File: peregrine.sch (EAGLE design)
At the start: 77 parts, among them IC2 LMV358IDGKR, J1 USB MICRO, Q1 BSS123, Q10 BSS123, Q11 BSS123, Q2 BSS123, U1 ITG-3200, U2 ADXL345, U5 ATMEGA32U4-XUAU, Y1 16MHz KX-7

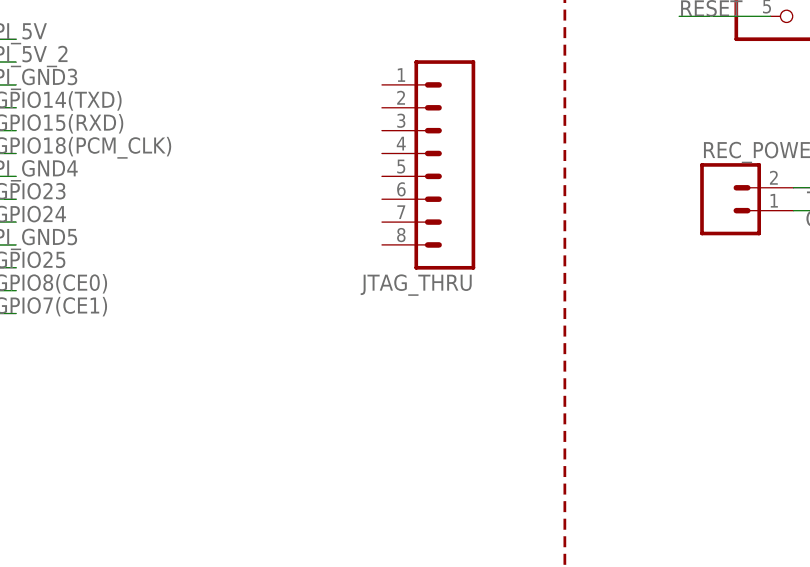
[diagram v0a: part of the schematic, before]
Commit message: Fixed silk
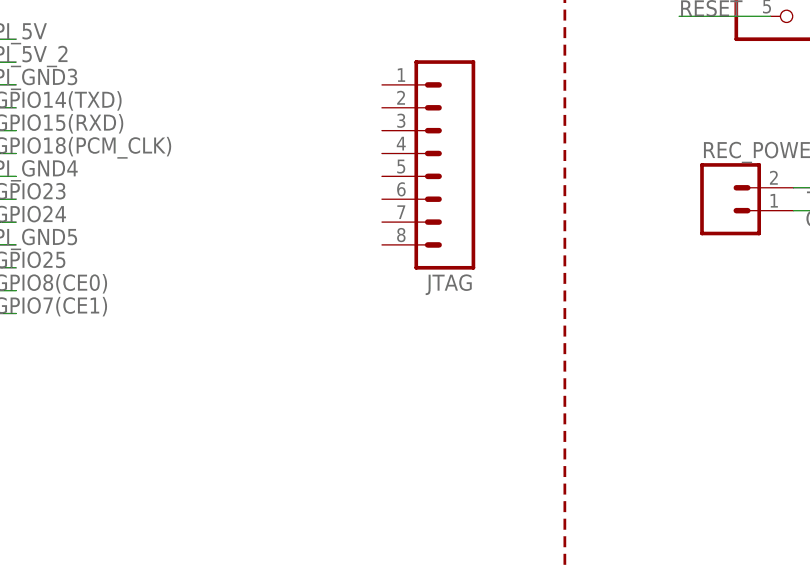
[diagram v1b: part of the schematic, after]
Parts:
- renumbered JTAG_THRU to JTAG
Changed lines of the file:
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@@
 <part name="C14" library="SparkFun" deviceset="CAP" device="0402-CAP" value="0.1uF"/>
 <part name="GND16" library="SparkFun" deviceset="GND" device=""/>
-<part name="JTAG_THRU" library="SparkFun" deviceset="M08" device="LOCK"/>
+<part name="JTAG" library="SparkFun" deviceset="M08" device="LOCK"/>
 <part name="SJ5" library="jumper" deviceset="SJ" device=""/>
 <part name="SJ6" library="jumper" deviceset="SJ" device=""/>
@@
 </instance>
 <instance part="GND16" gate="1" x="-15.24" y="-43.18"/>
-<instance part="JTAG_THRU" gate="G$1" x="124.46" y="83.82" rot="R180"/>
+<instance part="JTAG" gate="G$1" x="124.46" y="83.82" rot="R180"/>
 <instance part="SJ5" gate="1" x="231.14" y="48.26"/>
 <instance part="SJ6" gate="1" x="231.14" y="43.18"/>

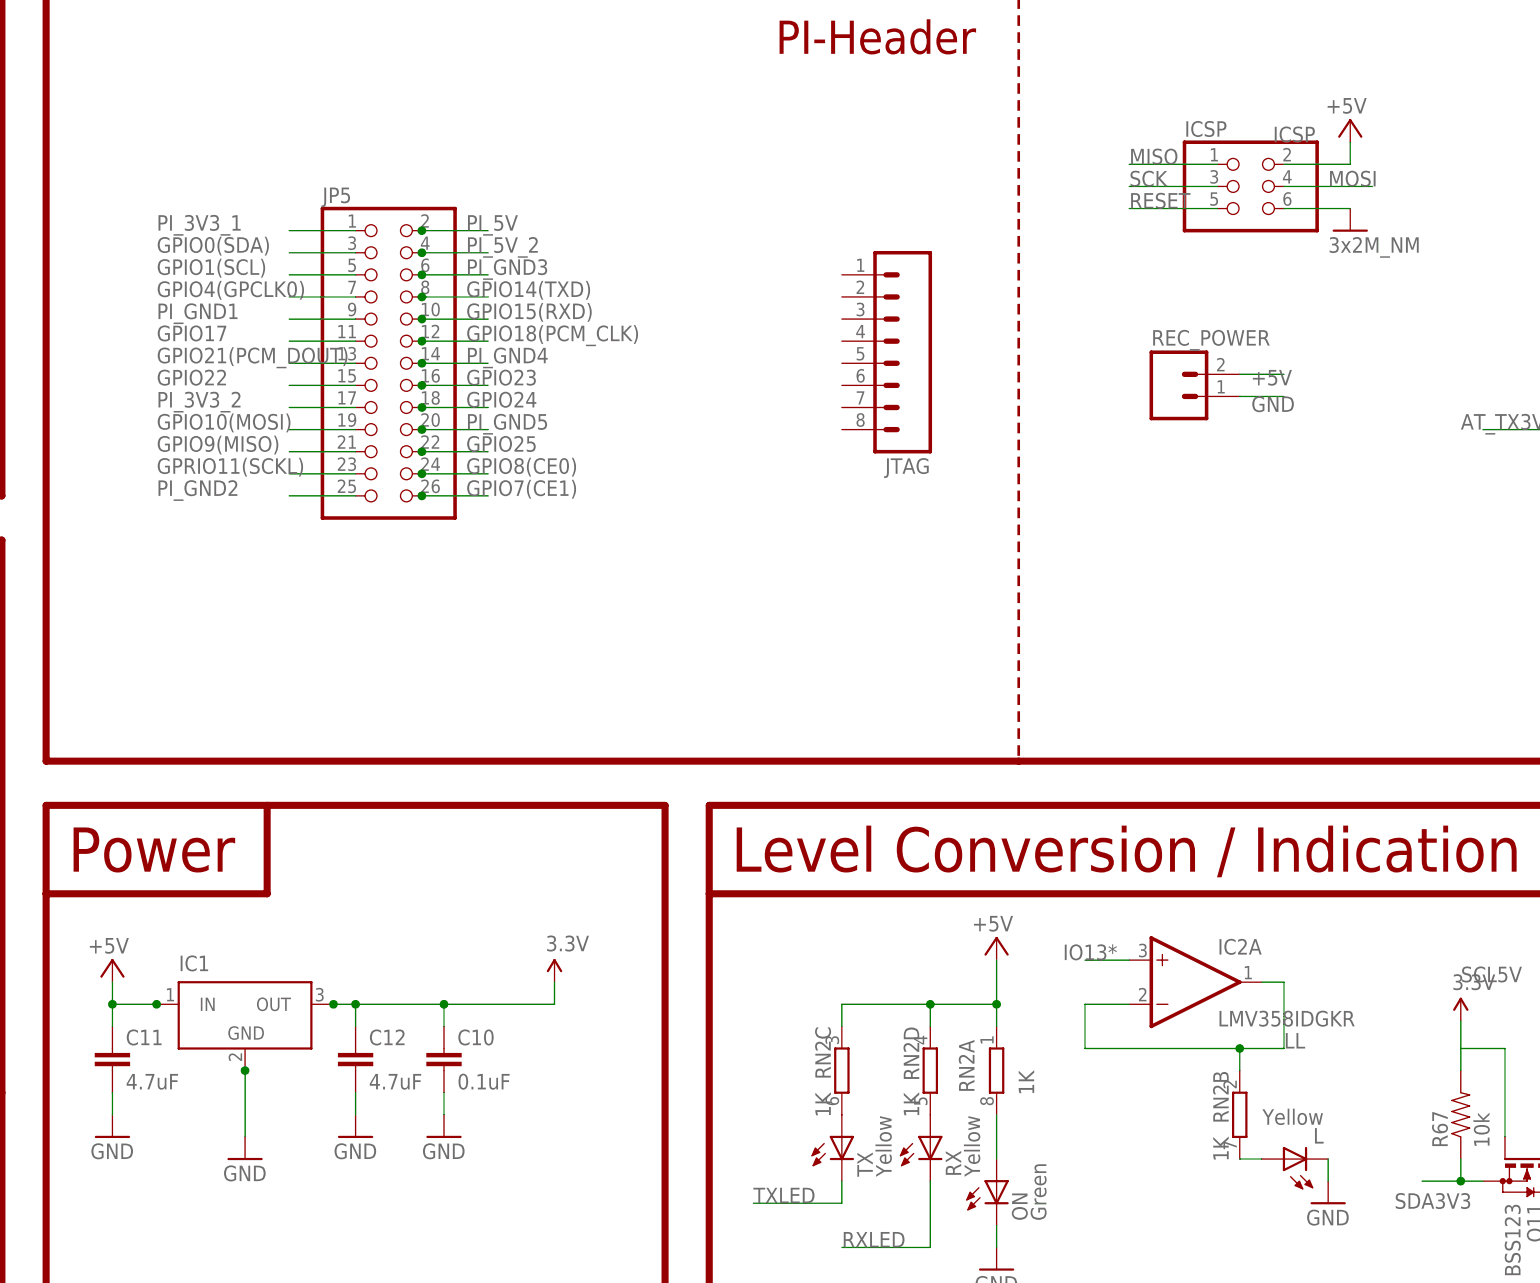
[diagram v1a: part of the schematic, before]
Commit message: Moderate Re-Route.`
Everything on top layer, a bit more pretty, some schematic changes, new
silk.
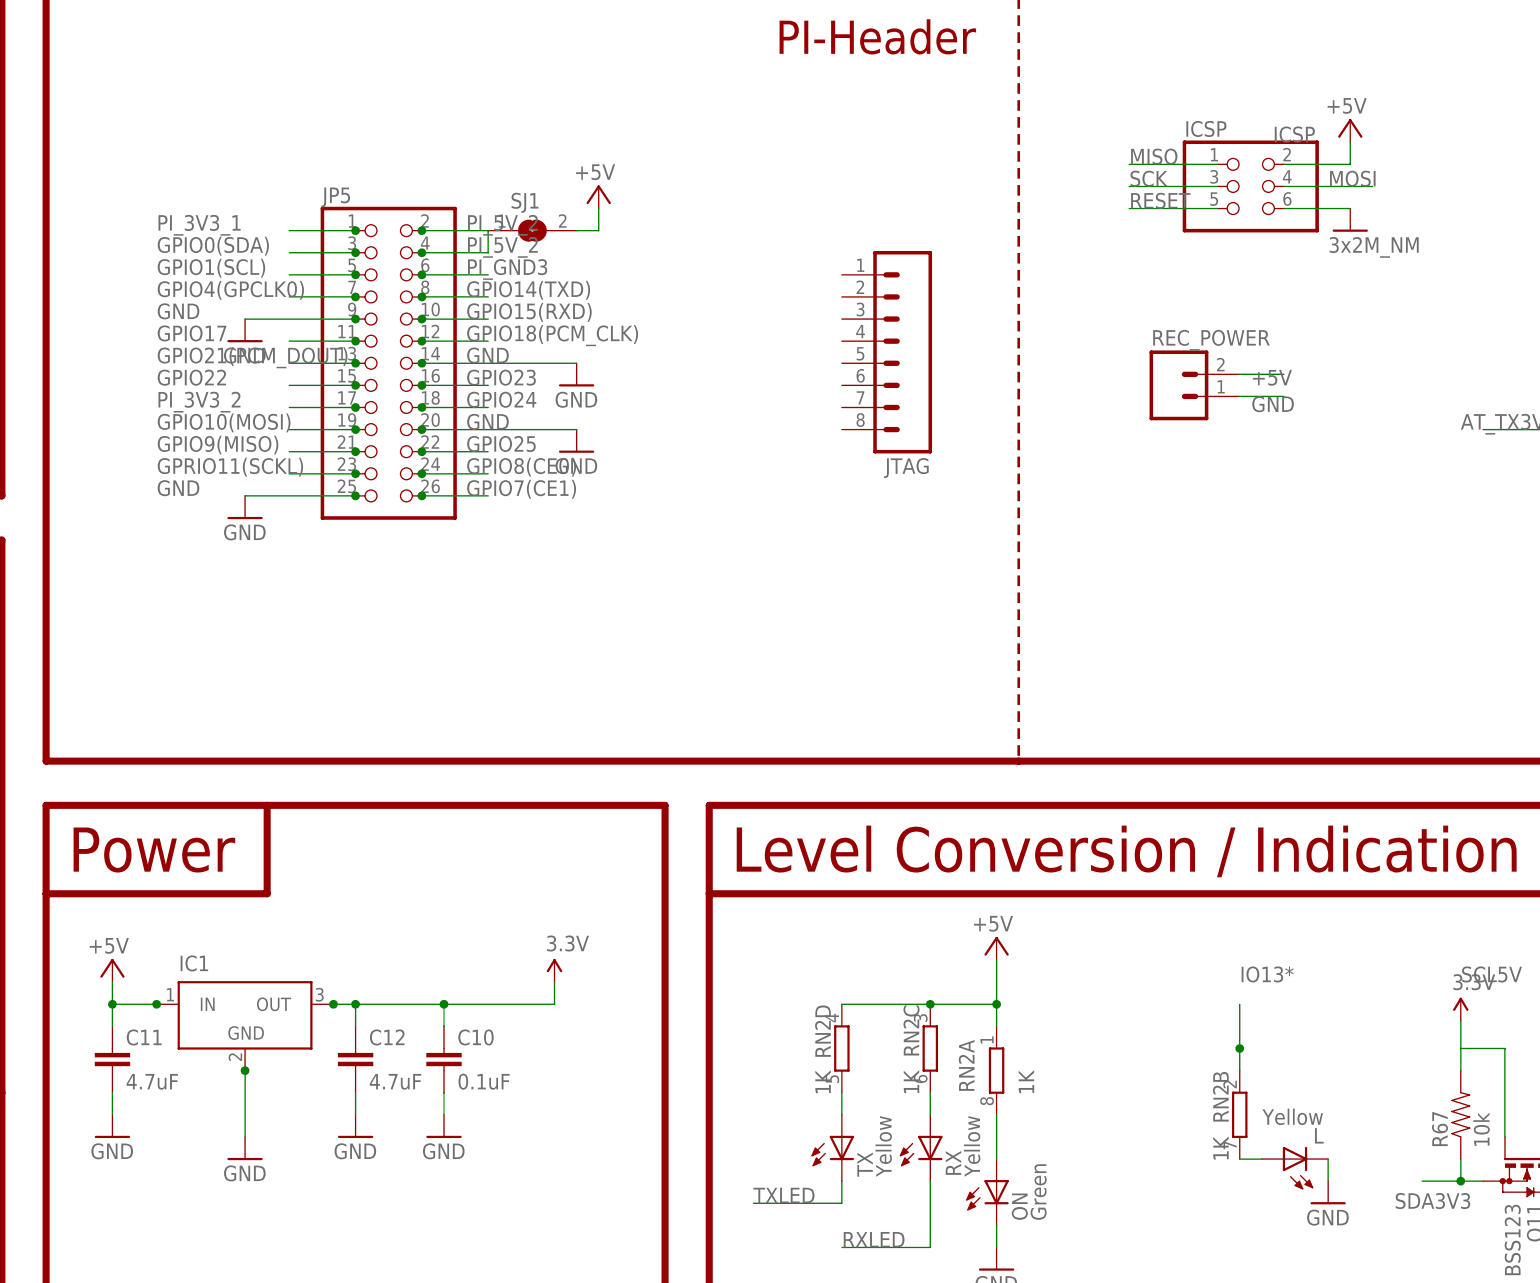
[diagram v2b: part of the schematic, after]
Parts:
- removed IC2: LMV358IDGKR, linear:LMV358MMX
- added SJ1: (no value), jumper:SJ
- R6, R7: device SmartPrj:R-EU_R0402 -> SmartPrj:R-EU_R0603
- REC: device SparkFun:M06LOCK -> SparkFun:M06SIP
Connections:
- removed net LL: IC2A.-IN, IC2A.OUT, RN2B.1
- removed net N$11: RN2C.2, TX.A
- removed net N$12: RN2D.2, RX.A
- removed net PI_5V: JP5.2
- removed net PI_GND1: JP5.9
- removed net PI_GND2: JP5.25
- removed net PI_GND4: JP5.14
- removed net PI_GND5: JP5.20
- new net N$10: RN2C.2, RX.A
- new net N$4: RN2D.2, TX.A
- net +5V: now also SJ1.2
- net GND: now also JP5.14, JP5.20, JP5.25, JP5.9
- net IO13*: now also RN2B.1; no longer IC2A.+IN
- net PI_5V_2: now also JP5.2, SJ1.1
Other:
- moved on the sheet: RN2C, RN2D

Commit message: Not a change, Just including version of board which was sent out.
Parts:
- removed J1: USB MICRO, SmartPrj:MYCON2_USB-MINI-B
- added X2: USB-MICROB, SparkFun:USB-MICROB
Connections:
- removed net USBID: J1.ID
- net D+: now also X2.D+; no longer J1.D+
- net D-: now also X2.D-; no longer J1.D-
- net GND: now also X2.GND; no longer J1.SH1, J1.SH2, J1.SH3, J1.SH4, J1.SH5, J1.SH6
- net UGND: no longer J1.GND
- net XUSB: now also X2.VBUS; no longer J1.VBUS
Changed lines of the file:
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@@
 <part name="Y1" library="SmartPrj" deviceset="CRYSTAL-3.2-2.5" device="" value="16MHz KX-7"/>
 <part name="D2" library="diode" deviceset="DIODE-" device="MINIMELF" value="CD1206-S01575"/>
-<part name="J1" library="SmartPrj" deviceset="MYCON2_USB-MINI-B" device="" value="USB MICRO"/>
 <part name="GND51" library="supply1" deviceset="GND" device=""/>
 <part name="U$3" library="SparkFun" deviceset="BMP085" device=""/>
@@
 <part name="GND17" library="SparkFun" deviceset="GND" device=""/>
 <part name="GND19" library="SparkFun" deviceset="GND" device=""/>
+<part name="X2" library="SparkFun" deviceset="USB" device="-MICROB"/>
 </parts>
 <sheets>
@@
 <attribute name="VALUE" x="-119.6086" y="152.4" size="1.778" layer="96" rot="R90"/>
 </instance>
-<instance part="J1" gate="G$1" x="175.26" y="175.26" rot="MR0"/>
 <instance part="GND51" gate="1" x="190.5" y="144.78"/>
 <instance part="U$3" gate="G$1" x="-40.64" y="-33.02"/>
@@
 <instance part="GND17" gate="1" x="88.9" y="71.12"/>
 <instance part="GND19" gate="1" x="88.9" y="78.74"/>
+<instance part="X2" gate="G$1" x="175.26" y="182.88" rot="R180"/>
 </instances>
 <busses>
@@
 </segment>
 <segment>
-<wire x1="162.56" y1="170.18" x2="160.02" y2="170.18" width="0.1524" layer="91"/>
-<wire x1="160.02" y1="172.72" x2="160.02" y2="170.18" width="0.1524" layer="91"/>
-<wire x1="162.56" y1="172.72" x2="160.02" y2="172.72" width="0.1524" layer="91"/>
-<wire x1="160.02" y1="175.26" x2="160.02" y2="172.72" width="0.1524" layer="91"/>
-<wire x1="162.56" y1="175.26" x2="160.02" y2="175.26" width="0.1524" layer="91"/>
-<wire x1="160.02" y1="177.8" x2="160.02" y2="175.26" width="0.1524" layer="91"/>
-<wire x1="162.56" y1="177.8" x2="160.02" y2="177.8" width="0.1524" layer="91"/>
 <wire x1="198.12" y1="152.4" x2="198.12" y2="147.32" width="0.1524" layer="91"/>
 <wire x1="198.12" y1="152.4" x2="198.12" y2="157.48" width="0.1524" layer="91"/>
@@
 <wire x1="208.28" y1="157.48" x2="208.28" y2="152.4" width="0.1524" layer="91"/>
 <wire x1="167.64" y1="157.48" x2="160.02" y2="157.48" width="0.1524" layer="91"/>
-<wire x1="160.02" y1="157.48" x2="160.02" y2="165.1" width="0.1524" layer="91"/>
-<wire x1="160.02" y1="165.1" x2="160.02" y2="167.64" width="0.1524" layer="91"/>
-<wire x1="160.02" y1="167.64" x2="160.02" y2="170.18" width="0.1524" layer="91"/>
 <wire x1="198.12" y1="147.32" x2="190.5" y2="147.32" width="0.1524" layer="91"/>
 <wire x1="190.5" y1="147.32" x2="160.02" y2="147.32" width="0.1524" layer="91"/>
 <wire x1="160.02" y1="147.32" x2="160.02" y2="157.48" width="0.1524" layer="91"/>
-<wire x1="162.56" y1="167.64" x2="160.02" y2="167.64" width="0.1524" layer="91"/>
-<wire x1="162.56" y1="165.1" x2="160.02" y2="165.1" width="0.1524" layer="91"/>
-<junction x="160.02" y="172.72"/>
-<junction x="160.02" y="175.26"/>
 <junction x="198.12" y="152.4"/>
-<junction x="160.02" y="170.18"/>
 <junction x="160.02" y="157.48"/>
-<junction x="160.02" y="167.64"/>
-<junction x="160.02" y="165.1"/>
 <junction x="190.5" y="147.32"/>
 <label x="160.02" y="177.8" size="1.778" layer="95" rot="MR0"/>
@@
 <pinref part="L2" gate="G$1" pin="2"/>
 <pinref part="Z2" gate="G$1" pin="2"/>
-<pinref part="J1" gate="G$1" pin="SH1"/>
-<pinref part="J1" gate="G$1" pin="SH2"/>
-<pinref part="J1" gate="G$1" pin="SH3"/>
-<pinref part="J1" gate="G$1" pin="SH4"/>
-<pinref part="J1" gate="G$1" pin="SH5"/>
-<pinref part="J1" gate="G$1" pin="SH6"/>
 <pinref part="GND51" gate="1" pin="GND"/>
+<pinref part="X2" gate="G$1" pin="GND"/>
+<wire x1="177.8" y1="182.88" x2="180.34" y2="182.88" width="0.1524" layer="91"/>
+<wire x1="180.34" y1="182.88" x2="180.34" y2="190.5" width="0.1524" layer="91"/>
+<wire x1="180.34" y1="190.5" x2="160.02" y2="190.5" width="0.1524" layer="91"/>
+<wire x1="160.02" y1="190.5" x2="160.02" y2="157.48" width="0.1524" layer="91"/>
 </segment>
 <segment>
@@
 <segment>
 <wire x1="218.44" y1="177.8" x2="208.28" y2="177.8" width="0.1524" layer="91"/>
-<wire x1="208.28" y1="177.8" x2="187.96" y2="177.8" width="0.1524" layer="91"/>
+<wire x1="208.28" y1="177.8" x2="177.8" y2="177.8" width="0.1524" layer="91"/>
 <wire x1="218.44" y1="177.8" x2="218.44" y2="180.34" width="0.1524" layer="91"/>
 <wire x1="208.28" y1="167.64" x2="208.28" y2="177.8" width="0.1524" layer="91"/>
@@
 <pinref part="Z2" gate="G$1" pin="1"/>
 <pinref part="RN3" gate="D" pin="2"/>
-<pinref part="J1" gate="G$1" pin="D-"/>
+<pinref part="X2" gate="G$1" pin="D-"/>
 </segment>
 </net>
@@
 <segment>
 <wire x1="218.44" y1="175.26" x2="198.12" y2="175.26" width="0.1524" layer="91"/>
-<wire x1="198.12" y1="175.26" x2="187.96" y2="175.26" width="0.1524" layer="91"/>
 <wire x1="218.44" y1="175.26" x2="218.44" y2="172.72" width="0.1524" layer="91"/>
 <wire x1="198.12" y1="167.64" x2="198.12" y2="175.26" width="0.1524" layer="91"/>
@@
 <pinref part="Z1" gate="G$1" pin="1"/>
 <pinref part="RN3" gate="A" pin="2"/>
-<pinref part="J1" gate="G$1" pin="D+"/>
+<pinref part="X2" gate="G$1" pin="D+"/>
+<wire x1="198.12" y1="175.26" x2="177.8" y2="175.26" width="0.1524" layer="91"/>
 </segment>
 </net>
@@
 <pinref part="L2" gate="G$1" pin="1"/>
 <pinref part="SUPPLY1" gate="G$1" pin="GND1"/>
-<pinref part="J1" gate="G$1" pin="GND"/>
+<label x="185.42" y="157.48" size="1.778" layer="95"/>
 </segment>
 </net>
 <net name="XUSB" class="3">
 <segment>
-<wire x1="187.96" y1="180.34" x2="195.58" y2="180.34" width="0.1524" layer="91"/>
 <label x="195.58" y="180.34" size="1.778" layer="95" rot="MR0"/>
 <pinref part="F1" gate="G$1" pin="2"/>
-<pinref part="J1" gate="G$1" pin="VBUS"/>
+<pinref part="X2" gate="G$1" pin="VBUS"/>
+<wire x1="195.58" y1="180.34" x2="177.8" y2="180.34" width="0.1524" layer="91"/>
 </segment>
 </net>
@@
 <wire x1="195.58" y1="172.72" x2="187.96" y2="172.72" width="0.1524" layer="91"/>
 <label x="195.58" y="172.72" size="1.778" layer="95" rot="MR0"/>
-<pinref part="J1" gate="G$1" pin="ID"/>
-</segment>
-</net>
+<label x="193.04" y="172.72" size="1.778" layer="95" rot="R180"/>
+</segment>
+</net>

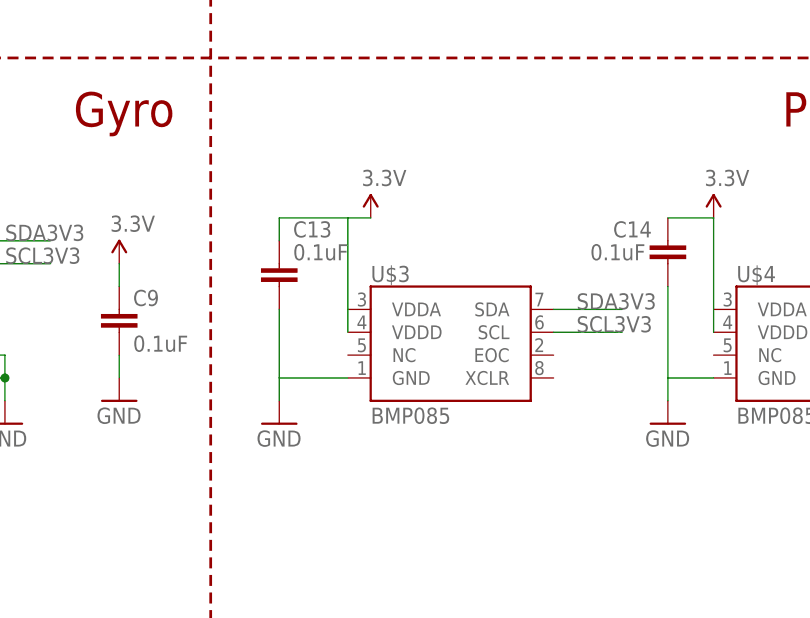
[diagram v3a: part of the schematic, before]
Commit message: Made room in layout for cutout
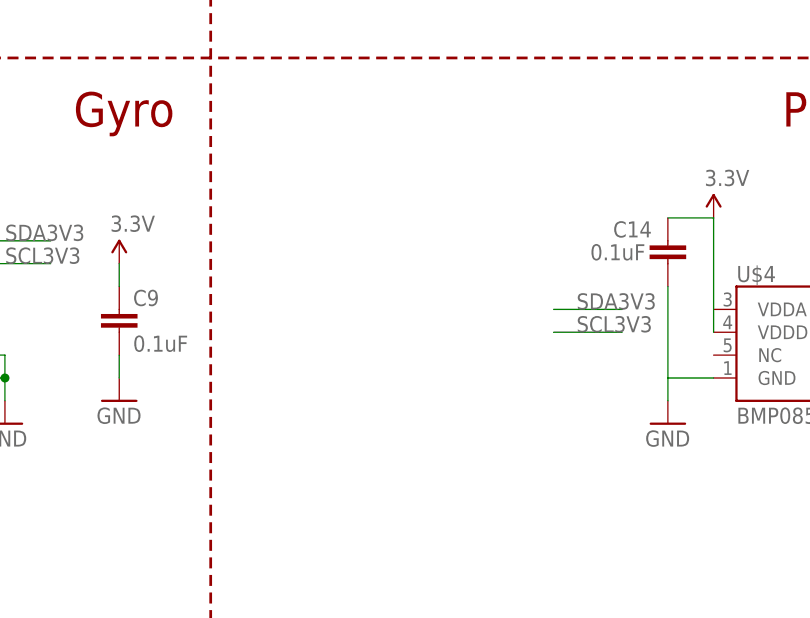
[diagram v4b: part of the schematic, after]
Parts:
- removed C13: 0.1uF, SparkFun:CAP0402-CAP
- removed U$3: BMP085, SparkFun:BMP085
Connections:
- net 3V3: no longer C13.1, U$3.VDDA, U$3.VDDD
- net GND: no longer C13.2, U$3.GND
- net SCL3V3: no longer U$3.SCL
- net SDA3V3: no longer U$3.SDA
